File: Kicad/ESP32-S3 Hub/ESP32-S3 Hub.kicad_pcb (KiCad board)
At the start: 6 copper layers, 15 x 30 mm, 60 parts, among them J1 1.27mm 3pin socket, J10 1.27mm 3pin socket, J11 7 pin FPC 0.3mm Panasonic Y3b, J12 1.27mm 3pin socket, J13 TE 3-2363961-0 receptacle, J14 TE 3-2363962-0 Connector, J16 TE 3-2363961-0 receptacle, J17 TE 3-2363962-0 Connector, J2 1.27mm 3pin socket, J21 1.27mm 4 pin socket, J22 1.27mm 4 pin header, J3 7 pin FPC 0.3mm Panasonic Y3b, J4 1.27mm 3pin socket, J5 7 pin FPC 0.3mm Panasonic Y3b, J6 1.27mm 3pin socket, J7 1.27mm 3pin socket, J8 7 pin FPC 0.3mm Panasonic Y3b, J9 1.27mm 3pin socket, SW1 Mitsumi R-667996, SW2 Mitsumi R-667996, U1 ESP32-S3, U2 74HC595, U3 THVD1420DRLR, Y1 ABM11-40.000MHZ-B1U-T3, 10ppm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

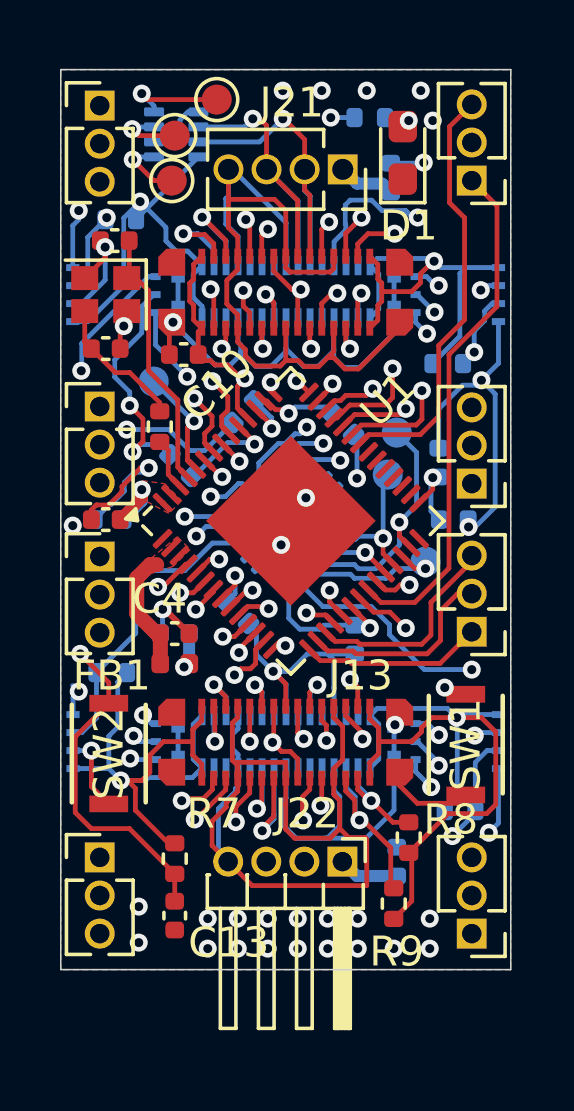
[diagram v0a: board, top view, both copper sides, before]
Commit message: Fixed DRC errors
There were a lot of board clearance issues with the magnetic sensor connectors. I had to change the copper to edge distance to 0.28mm from 0.3, as well as move the connectors a smidge back from the edge.
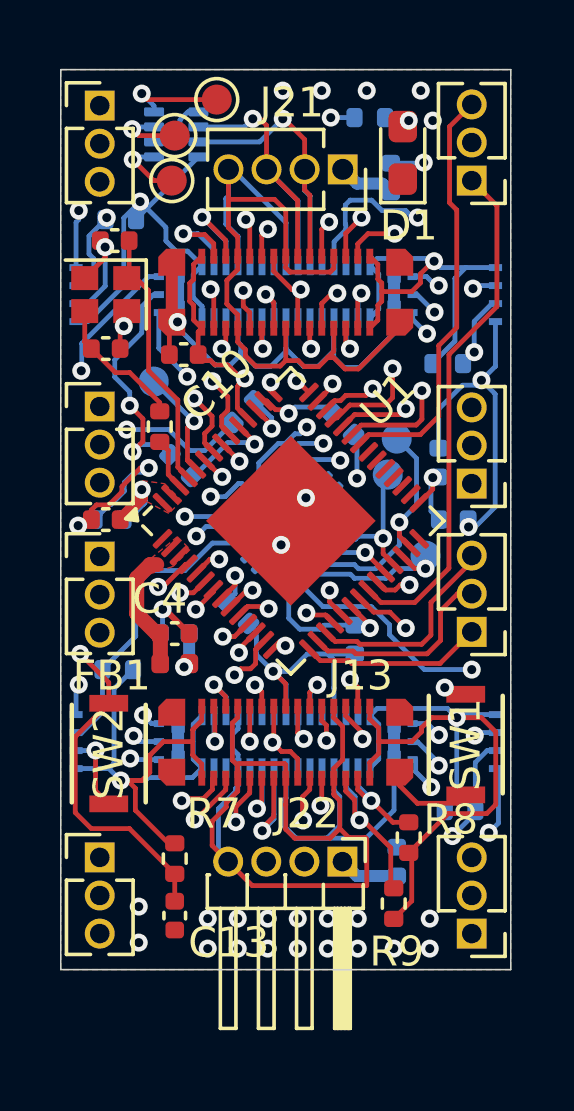
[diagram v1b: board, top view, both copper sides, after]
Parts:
- moved R18 0.22 mm to (149.8, 101.8)
- moved TP14 0.20 mm to (160.1, 98.0)
- moved TP1 0.20 mm to (159.1, 94.1)
- moved J11 0.11 mm to (149.7, 89.3)
- moved J3 0.10 mm to (161.1, 104.2)
- moved J5 0.10 mm to (149.7, 104.2)
- moved J8 0.10 mm to (161.1, 89.3)
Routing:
- net GND: track 149.2 -> 150.8 mm, vias 42 -> 41
- net MOSI1: track 89.2 -> 88.4 mm
- net LED: track 23.8 -> 24.5 mm

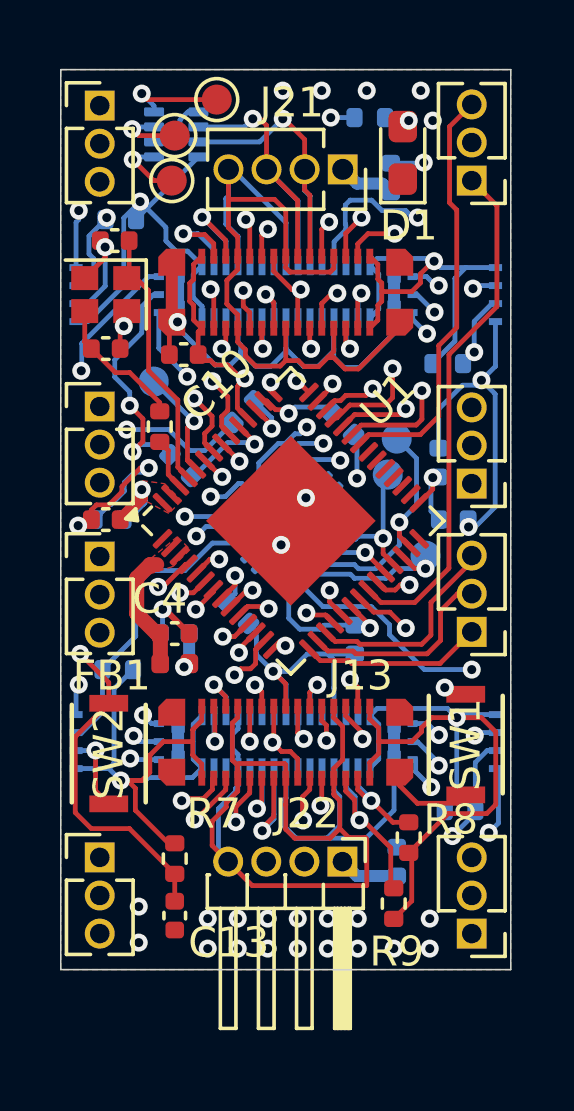
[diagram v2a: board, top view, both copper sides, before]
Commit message: Fixed OE pin by adding pullup, updated silkscreen
The silkscreen looks really nice now, I have all the port labels.
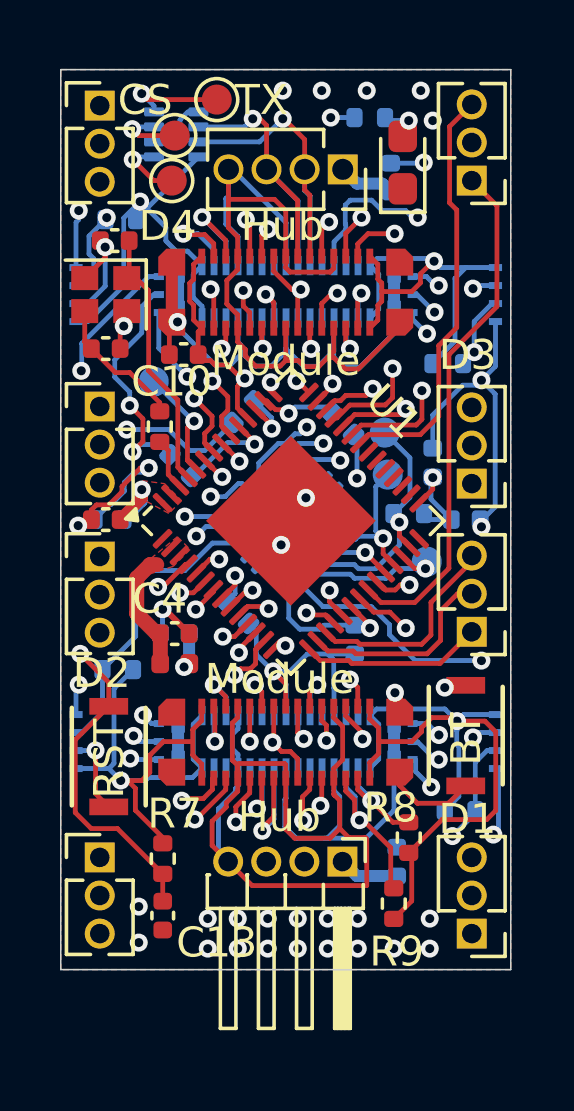
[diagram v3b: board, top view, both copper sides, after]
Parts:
- added R11: 10k, Resistor_SMD:R_0402_1005Metric, B.Cu at (159.5, 96.6)
- C3: value 1uF -> 0.1uF
- moved TP1 0.45 mm to (158.7, 93.9)
- moved C5 0.40 mm to (161.4, 96.8)
- moved C13 0.40 mm to (151.3, 110.0)
- moved R7 0.40 mm to (151.3, 108.1)
- moved D1 0.33 mm to (159.3, 84.9)
- moved SW1 0.30 mm to (161.4, 104.0)
- moved TP14 0.20 mm to (160.1, 98.2)
- moved C7 0.20 mm to (160.3, 94.9)
- moved SW2 0.10 mm to (149.5, 104.7)
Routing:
- net VDD: track 175.8 -> 176.9 mm
- net GND: track 150.8 -> 151.6 mm, vias 41 -> 42
- net NRST: track 16.6 -> 16.0 mm
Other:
- board text added: "3v3"
- board text added: "BT"
- board text added: "CS"
- board text added: "D+"
- board text added: "D-"
- board text added: "D1"
- board text added: "D2"
- board text added: "D3"
- board text added: "D4"
- board text added: "GND"
- board text added: "Hub"
- board text added: "IO46"
- board text added: "Module"
- board text added: "RST"
- board text added: "S+"
- board text added: "S-"
- board text added: "SEN"
- board text added: "SPI"
- board text added: "TX"

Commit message: Fixed left side swapped headers, tuned RS485 skew
The left side shouldn't have been mirrored, it should be rotated 180. I had to swap the CSA and the PWM output headers, which was a hassle. I also tuned the RS485 trace skews finally, something I forgot when I "finished" the board a month ago.
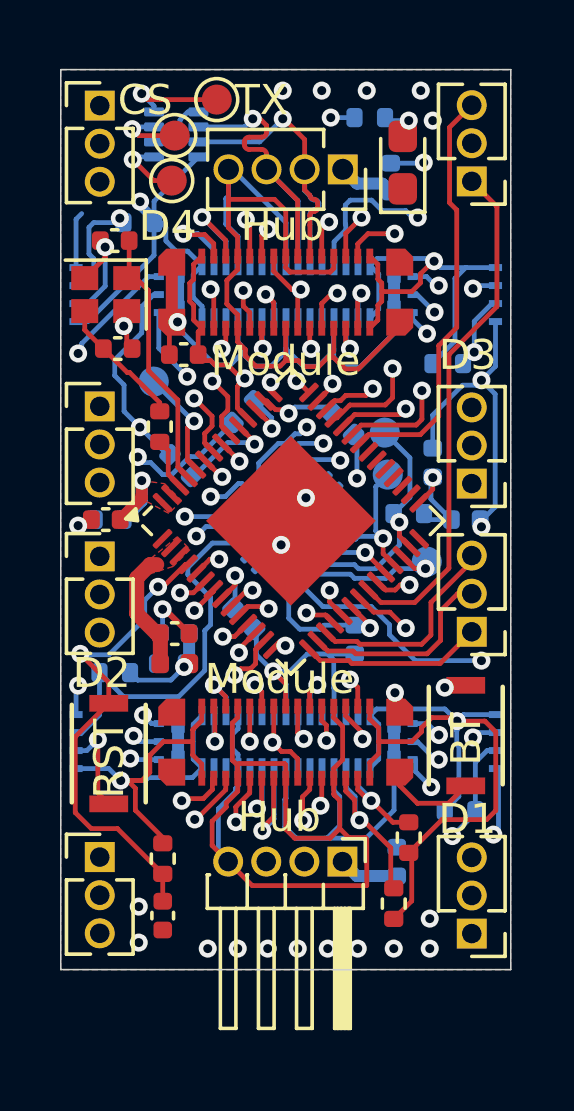
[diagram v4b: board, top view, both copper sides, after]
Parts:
- moved J6 10.0 mm to (149.2, 98.0)
- moved J12 10.0 mm to (149.2, 83.0)
- moved J10 10.0 mm to (149.2, 93.0)
- moved J4 10.0 mm to (149.2, 108.0)
- moved R20 0.61 mm to (150.5, 86.9)
- moved C11 0.40 mm to (149.8, 91.1)
- moved R1 0.28 mm to (154.0, 100.1)
- moved R18 0.14 mm to (149.7, 101.9)
- moved SW2 0.10 mm to (149.5, 104.6)
- moved C3 0.10 mm to (151.6, 101.6)
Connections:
- U1 pad 37: 4A -> 4C
- U1 pad 38: 4B -> 4A
- U1 pad 39: 4C -> 4B
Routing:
- net 4CSA-B: track 7.74 -> 19.2 mm
- net 4CSA-A: track 9.19 -> 19.6 mm
- net 2B: track 11.4 -> 21.6 mm
- net 2C: track 14.5 -> 23.3 mm
- net 4C: track 16.4 -> 24.3 mm
- net MISO1: track 101.5 -> 93.8 mm, vias 9 -> 8
- net 2CSA-B: track 13.8 -> 6.36 mm
- net 2A: track 10.3 -> 17.2 mm
- net GND: track 151.6 -> 146.1 mm, vias 42 -> 34
- net RS485-: track 57.0 -> 62.5 mm
- net 2CSA-A: track 11.9 -> 6.69 mm
- net RS485+: track 57.9 -> 62.0 mm
- net CS2: track 10.4 -> 13.0 mm
- net 4A: track 21.8 -> 19.5 mm
- net 4B: track 19.6 -> 17.4 mm
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
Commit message: Tweaked some tracks
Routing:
- net RS485-: track 62.5 -> 64.4 mm, vias 4 -> 3

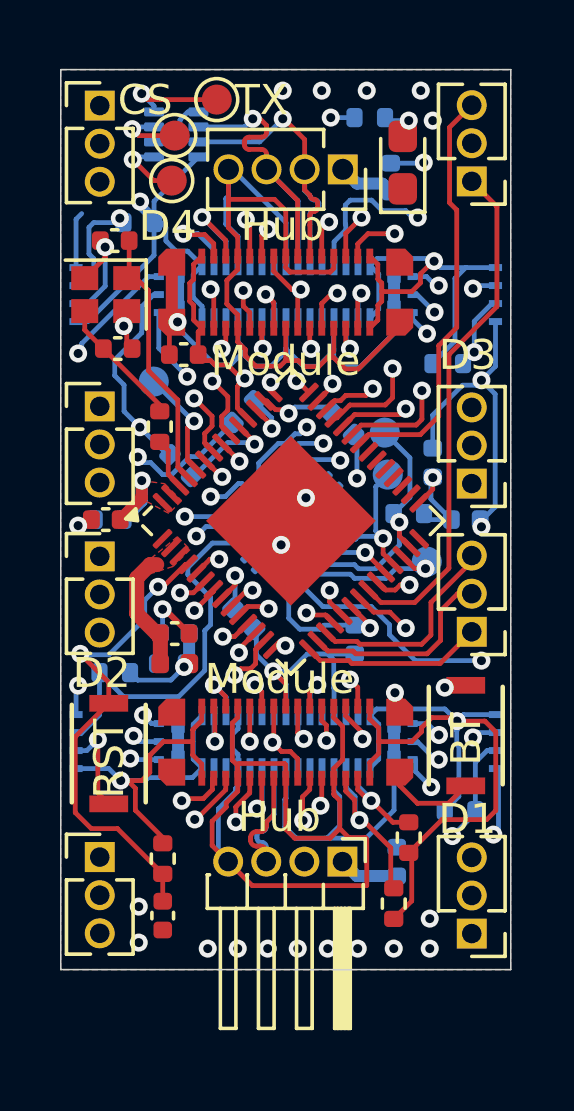
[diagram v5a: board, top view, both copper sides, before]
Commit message: Fixed headers and connectors miss-alignments
Almost everything was misaligned. The holes on the hub to hub headers must be 2.9mm from the edge, the header holes on the motor drivers must be 4.5mm from the edge, and the centers of the power connectors(either gender) must be 2.15mm from the edge
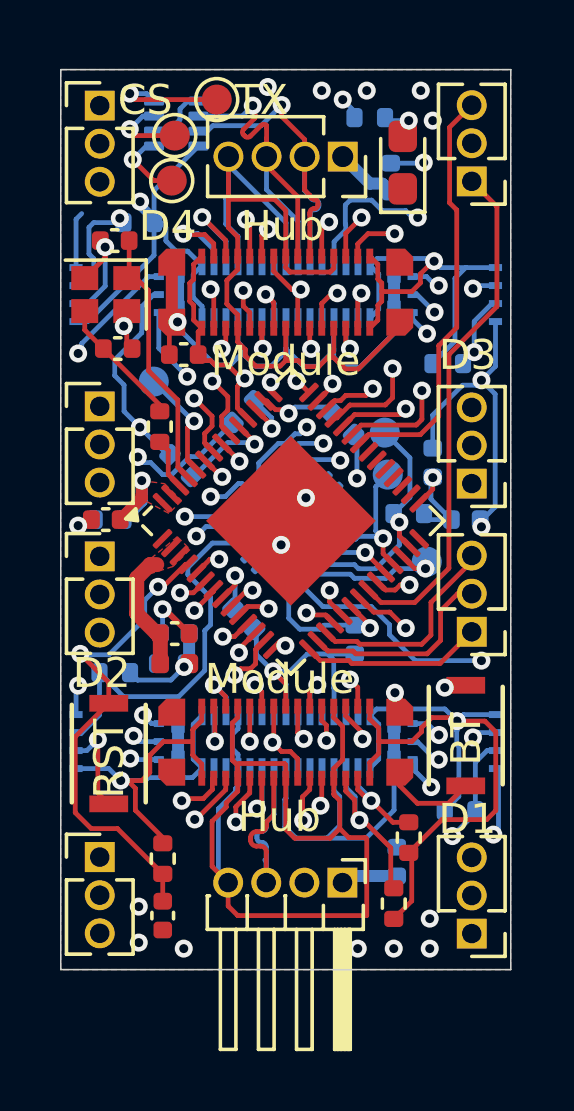
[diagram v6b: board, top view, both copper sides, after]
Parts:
- moved J22 0.70 mm to (157.3, 108.9)
- moved J21 0.42 mm to (157.3, 84.7)
- moved U3 0.36 mm to (151.8, 83.6)
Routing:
- net VDD: track 177.1 -> 162.3 mm
- net RS485-: track 64.4 -> 69.0 mm
- net GND: track 146.1 -> 150.2 mm, vias 34 -> 30
- net RS485+: track 62.0 -> 65.4 mm
- net MISO1: track 94.1 -> 95.5 mm
- net MOSI1: track 88.2 -> 89.5 mm
- net CS8: track 31.2 -> 32.3 mm
- net CS7: track 31.2 -> 32.3 mm
- net UART0_TX: track 18.4 -> 19.1 mm

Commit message: Added LCSC part numbers, DNP attr, and exported Gerbers
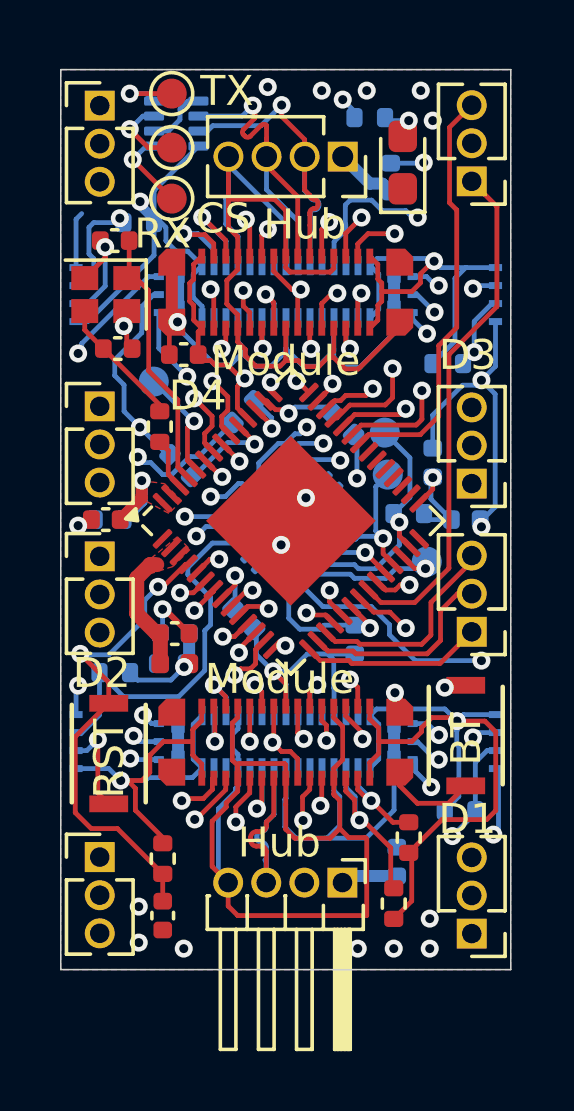
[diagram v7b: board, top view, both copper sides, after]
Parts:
- D1: value Osram LT Q99G.01 green led -> 2.6~3.1 Fv Green 5ma
- moved TP3 1.51 mm to (151.6, 82.6)
- moved TP2 0.60 mm to (151.6, 86.1)
- moved TP20 0.41 mm to (151.6, 84.4)
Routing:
- net UART0_TX: track 19.1 -> 17.5 mm
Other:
- board text added: "RX"
